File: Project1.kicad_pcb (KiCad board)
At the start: 2 copper layers, 49 parts, among them IC1 LM324N, IC2 LM324N, IC3 LM324N, IC4 LM324N

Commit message: 0518 final edited.
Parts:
- moved R19 65.0 mm to (43.7, 59.3)
- moved R20 65.0 mm to (43.7, 61.8)
- moved R21 60.1 mm to (47.7, 41.7)
- moved R22 60.1 mm to (47.7, 44.2)
- moved R23 60.1 mm to (47.7, 46.7)
- moved R24 60.1 mm to (47.7, 49.2)
- moved C6 59.8 mm to (31.7, 54.3)
- moved C7 59.8 mm to (31.7, 56.8)
- moved C8 59.8 mm to (31.7, 59.3)
- moved R10 59.8 mm to (39.7, 59.3)
- moved R8 59.8 mm to (39.7, 54.3)
- moved R9 59.8 mm to (39.7, 56.8)
- moved C5 59.8 mm to (31.7, 51.8)
- moved C9 59.8 mm to (31.7, 61.8)
- moved R11 59.8 mm to (39.7, 61.8)
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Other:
- board outline added: 100 x 100 mm

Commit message: 0520 Edited.
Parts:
- removed BZ1: Buzzer, Buzzer_Beeper:Buzzer_12x9.5RM7.6
- removed S1, S2, S3, S4: DS01-254-L-01BE, Project1:SW_DS01-254-L-01BE
- added D1: LED, LED_THT:LED_D3.0mm, F.Cu at (51.0, 35.9)
- added D2: LED, LED_THT:LED_D3.0mm, F.Cu at (51.0, 41.3)
- added D3: LED, LED_THT:LED_D3.0mm, F.Cu at (51.0, 46.8)
- added D4: LED, LED_THT:LED_D3.0mm, F.Cu at (51.0, 52.3)
- added IC5: LM324N, Project1:LM324N, F.Cu at (62.5, 22.8)
- added IC6: LM324N, Project1:LM324N, F.Cu at (73.4, 22.8)
- added Q1: Q_NPN, Project1:TNPN_TO-92_ONS, F.Cu at (42.4, 36.0)
- added Q2: Q_NPN, Project1:TNPN_TO-92_ONS, F.Cu at (42.4, 41.8)
- added Q3: Q_NPN, Project1:TNPN_TO-92_ONS, F.Cu at (42.4, 47.7)
- added Q4: Q_NPN, Project1:TNPN_TO-92_ONS, F.Cu at (42.4, 53.5)
- added R0: R, Resistor_SMD:R_0603_1608Metric, F.Cu at (19.1, 44.4)
- added R25: R, Resistor_SMD:R_0603_1608Metric, F.Cu at (27.2, 46.9)
- added R26: R, Resistor_SMD:R_0603_1608Metric, F.Cu at (27.2, 49.5)
- added R27: R, Resistor_SMD:R_0603_1608Metric, F.Cu at (27.2, 52.0)
- added R28: R, Resistor_SMD:R_0603_1608Metric, F.Cu at (27.2, 54.5)
- added R29: R, Resistor_SMD:R_0603_1608Metric, F.Cu at (27.2, 57.0)
- added R30: R, Resistor_SMD:R_0603_1608Metric, F.Cu at (27.2, 59.5)
- added R31: R, Resistor_SMD:R_0603_1608Metric, F.Cu at (27.2, 62.0)
- added R32: R, Resistor_SMD:R_0603_1608Metric, F.Cu at (31.2, 34.4)
- added R33: R, Resistor_SMD:R_0603_1608Metric, F.Cu at (31.2, 36.9)
- added R34: R, Resistor_SMD:R_0603_1608Metric, F.Cu at (31.2, 39.4)
- added R35: R, Resistor_SMD:R_0603_1608Metric, F.Cu at (31.2, 41.9)
- added R36: R, Resistor_SMD:R_0603_1608Metric, F.Cu at (31.2, 44.4)
- added R37: R, Resistor_SMD:R_0603_1608Metric, F.Cu at (31.2, 46.9)
- added R38: R, Resistor_SMD:R_0603_1608Metric, F.Cu at (31.2, 49.5)
- added R39: R, Resistor_SMD:R_0603_1608Metric, F.Cu at (31.2, 52.0)
- added R40: R, Resistor_SMD:R_0603_1608Metric, F.Cu at (31.2, 54.5)
- added R41: R, Resistor_SMD:R_0603_1608Metric, F.Cu at (31.2, 57.0)
- added R42: R, Resistor_SMD:R_0603_1608Metric, F.Cu at (31.2, 59.5)
- added R43: R, Resistor_SMD:R_0603_1608Metric, F.Cu at (31.2, 62.0)
- added R44: R, Resistor_SMD:R_0603_1608Metric, F.Cu at (35.2, 34.4)
- added R45: R, Resistor_SMD:R_0603_1608Metric, F.Cu at (35.2, 36.9)
- added R46: R, Resistor_SMD:R_0603_1608Metric, F.Cu at (35.2, 39.4)
- added R47: R, Resistor_SMD:R_0603_1608Metric, F.Cu at (35.2, 41.9)
- added R48: R, Resistor_SMD:R_0603_1608Metric, F.Cu at (35.2, 44.4)
- added R49: R, Resistor_SMD:R_0603_1608Metric, F.Cu at (35.2, 46.9)
- added R50: R, Resistor_SMD:R_0603_1608Metric, F.Cu at (35.2, 49.5)
- added R51: R, Resistor_SMD:R_0603_1608Metric, F.Cu at (35.2, 52.0)
- added R52: R, Resistor_SMD:R_0603_1608Metric, F.Cu at (35.2, 54.5)
- added R53: R, Resistor_SMD:R_0603_1608Metric, F.Cu at (35.2, 57.0)
- added R54: R, Resistor_SMD:R_0603_1608Metric, F.Cu at (35.2, 59.5)
- added R55: R, Resistor_SMD:R_0603_1608Metric, F.Cu at (35.2, 62.0)
- added R56: R, Resistor_SMD:R_0603_1608Metric, F.Cu at (39.2, 34.4)
- added R57: R, Resistor_SMD:R_0603_1608Metric, F.Cu at (39.2, 36.9)
- added R58: R, Resistor_SMD:R_0603_1608Metric, F.Cu at (39.2, 39.4)
- added R59: R, Resistor_SMD:R_0603_1608Metric, F.Cu at (39.2, 41.9)
- added R60: R, Resistor_SMD:R_0603_1608Metric, F.Cu at (39.2, 44.4)
- added R61: R, Resistor_SMD:R_0603_1608Metric, F.Cu at (39.2, 46.9)
- added R62: R, Resistor_SMD:R_0603_1608Metric, F.Cu at (39.2, 49.5)
- added R63: R, Resistor_SMD:R_0603_1608Metric, F.Cu at (39.2, 52.0)
- moved R20 32.0 mm to (27.2, 34.4)
- moved R10 25.9 mm to (23.1, 39.4)
- moved R8 25.9 mm to (23.1, 34.4)
- moved R9 25.9 mm to (23.1, 36.9)
- moved R11 25.9 mm to (23.1, 41.9)
- moved C11 25.6 mm to (15.1, 59.5)
- moved C10 25.6 mm to (15.1, 57.0)
- moved C12 25.6 mm to (15.1, 62.0)
- moved R3 23.0 mm to (19.1, 52.0)
- moved R4 23.0 mm to (19.1, 54.5)
- moved R6 23.0 mm to (19.1, 59.5)
- moved R7 23.0 mm to (19.1, 62.0)
- moved R5 23.0 mm to (19.1, 57.0)
- moved C15 22.2 mm to (19.1, 39.4)
- moved C13 22.2 mm to (19.1, 34.4)
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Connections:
- C1 pad 1: Net-(IC1-INPUT_2+) -> Net-(C1-Pad1)
- C1 pad 2: Net-(C1-Pad2) -> Net-(IC1-INPUT_3+)
- C10 pad 2: Net-(IC3-INPUT_1-) -> Net-(IC4-INPUT_2-)
- C11 pad 2: Net-(IC3-INPUT_4+) -> Net-(IC4-INPUT_4-)
- C12 pad 2: Net-(IC3-INPUT_3-) -> Net-(IC4-INPUT_3+)
- C13 pad 1: Net-(IC4-INPUT_2+) -> Net-(IC6-INPUT_2-)
- C14 pad 2: Net-(IC4-INPUT_1-) -> Net-(IC6-INPUT_2-)
- C15 pad 2: Net-(IC4-INPUT_4+) -> Net-(IC6-INPUT_4-)
- C16 pad 2: Net-(IC4-INPUT_3-) -> Net-(IC6-INPUT_3+)
- C2 pad 1: Net-(C1-Pad2) -> Net-(C1-Pad1)
- C2 pad 2: Net-(IC1-INPUT_1-) -> Net-(IC1-INPUT_4-)
- C3 pad 2: Net-(IC1-INPUT_4+) -> Net-(IC1-INPUT_2-)
- C4 pad 1: Net-(C3-Pad1) -> Net-(IC1-OUTPUT_2)
- C4 pad 2: Net-(IC1-INPUT_3-) -> Net-(C3-Pad1)
- C5 pad 1: Net-(IC2-INPUT_2+) -> Net-(IC3-INPUT_2-)
- C6 pad 2: Net-(IC2-INPUT_1-) -> Net-(IC3-INPUT_2-)
- C7 pad 2: Net-(IC2-INPUT_4+) -> Net-(IC3-INPUT_4-)
- C8 pad 2: Net-(IC2-INPUT_3-) -> Net-(IC3-INPUT_3+)
- C9 pad 1: Net-(IC3-INPUT_2+) -> Net-(IC4-OUTPUT_2)
- IC1 pad 1: Net-(IC1-INPUT_2+) -> Net-(IC1-INPUT_1-)
- IC1 pad 10: GND -> Net-(IC1-INPUT_3+)
- IC1 pad 11: GND -> -12V
- IC1 pad 12: Net-(IC1-INPUT_4+) -> GND
- IC1 pad 13: Net-(BZ1-+) -> Net-(IC1-INPUT_4-)
- IC1 pad 14: Net-(BZ1-+) -> Net-(IC1-INPUT_3+)
- IC1 pad 3: GND -> Net-(IC1-INPUT_1+)
- IC1 pad 4: +15V -> +12V
- IC1 pad 5: Net-(IC1-INPUT_2+) -> GND
- IC1 pad 7: Net-(IC1-INPUT_2-) -> Net-(IC1-OUTPUT_2)
- IC1 pad 8: Net-(IC1-INPUT_4+) -> Net-(IC1-INPUT_3-)
- IC2 pad 1: Net-(IC2-INPUT_2+) -> Net-(IC2-INPUT_1-)
- IC2 pad 10: GND -> Net-(IC2-INPUT_3+)
- IC2 pad 11: GND -> -12V
- IC2 pad 12: Net-(IC2-INPUT_4+) -> GND
- IC2 pad 13: Net-(BZ1-+) -> Net-(IC2-INPUT_4-)
- IC2 pad 14: Net-(BZ1-+) -> Net-(D1-A)
- IC2 pad 3: GND -> Net-(IC2-INPUT_1+)
- IC2 pad 4: +15V -> +12V
- IC2 pad 5: Net-(IC2-INPUT_2+) -> GND
- IC2 pad 7: Net-(IC2-INPUT_2-) -> Net-(D2-A)
- IC2 pad 8: Net-(IC2-INPUT_4+) -> Net-(IC2-INPUT_3-)
- IC3 pad 1: Net-(IC3-INPUT_2+) -> Net-(IC3-INPUT_1-)
- IC3 pad 10: GND -> Net-(IC3-INPUT_3+)
- IC3 pad 11: GND -> -12V
- IC3 pad 12: Net-(IC3-INPUT_4+) -> GND
- IC3 pad 13: Net-(BZ1-+) -> Net-(IC3-INPUT_4-)
- IC3 pad 14: Net-(BZ1-+) -> Net-(IC3-INPUT_3+)
- IC3 pad 3: GND -> Net-(IC3-INPUT_1+)
- IC3 pad 4: +15V -> +12V
- IC3 pad 5: Net-(IC3-INPUT_2+) -> GND
- IC3 pad 8: Net-(IC3-INPUT_4+) -> Net-(IC3-INPUT_3-)
- IC4 pad 1: Net-(IC4-INPUT_2+) -> Net-(IC4-INPUT_1-)
- IC4 pad 10: GND -> Net-(IC4-INPUT_3+)
- IC4 pad 11: GND -> -12V
- IC4 pad 12: Net-(IC4-INPUT_4+) -> GND
- IC4 pad 13: Net-(BZ1-+) -> Net-(IC4-INPUT_4-)
- IC4 pad 14: Net-(BZ1-+) -> Net-(IC4-INPUT_3+)
- IC4 pad 3: GND -> Net-(IC4-INPUT_1+)
- IC4 pad 4: +15V -> +12V
- IC4 pad 5: Net-(IC4-INPUT_2+) -> GND
- IC4 pad 7: Net-(IC4-INPUT_2-) -> Net-(IC4-OUTPUT_2)
- IC4 pad 8: Net-(IC4-INPUT_4+) -> Net-(IC4-INPUT_3-)
- R1 pad 1: Net-(R1-Pad1) -> Net-(IC1-INPUT_1-)
- R1 pad 2: Net-(C1-Pad2) -> Net-(R1-Pad2)
- R10 pad 1: Net-(IC2-INPUT_2-) -> Net-(R10-Pad1)
- R10 pad 2: Net-(C7-Pad1) -> Net-(IC1-OUTPUT_2)
- R11 pad 1: Net-(C7-Pad1) -> Net-(IC2-INPUT_1+)
- R12 pad 1: Net-(IC2-INPUT_4+) -> Net-(IC2-INPUT_1+)
- R12 pad 2: Net-(IC2-INPUT_3-) -> +12V
- R13 pad 1: Net-(R13-Pad1) -> Net-(IC2-INPUT_4-)
- R13 pad 2: Net-(C10-Pad1) -> Net-(IC2-INPUT_1-)
- R14 pad 1: Net-(C10-Pad1) -> Net-(IC2-INPUT_4-)
- R14 pad 2: GND -> -12V
- R15 pad 1: Net-(IC3-INPUT_2+) -> Net-(IC2-INPUT_4-)
- R15 pad 2: Net-(IC3-INPUT_1-) -> Net-(D1-A)
- R16 pad 1: Net-(IC3-INPUT_2-) -> Net-(R16-Pad1)
- R16 pad 2: Net-(C11-Pad1) -> Net-(IC3-INPUT_2-)
- R17 pad 1: Net-(C11-Pad1) -> Net-(IC3-INPUT_2-)
- R17 pad 2: GND -> Net-(R16-Pad1)
- R18 pad 1: Net-(IC3-INPUT_4+) -> Net-(R0-Pad1)
- R18 pad 2: Net-(IC3-INPUT_3-) -> Net-(IC3-INPUT_1+)
- R19 pad 1: Net-(R19-Pad1) -> Net-(IC2-INPUT_3+)
- R19 pad 2: Net-(C13-Pad2) -> +12V
- R2 pad 1: Net-(C1-Pad2) -> Net-(R1-Pad2)
- R2 pad 2: GND -> Net-(C1-Pad1)
- R20 pad 1: Net-(C13-Pad2) -> Net-(IC2-INPUT_3+)
- R21 pad 1: Net-(IC4-INPUT_2+) -> Net-(IC3-INPUT_1-)
- R21 pad 2: Net-(IC4-INPUT_1-) -> Net-(R21-Pad2)
- R22 pad 1: Net-(IC4-INPUT_2-) -> Net-(C5-Pad2)
- R22 pad 2: Net-(C15-Pad1) -> GND
- R23 pad 1: Net-(C15-Pad1) -> Net-(R23-Pad1)
- R23 pad 2: GND -> Net-(IC4-OUTPUT_2)
- R24 pad 1: Net-(IC4-INPUT_4+) -> Net-(R21-Pad2)
- R24 pad 2: Net-(IC4-INPUT_3-) -> Net-(C7-Pad1)
- R3 pad 1: Net-(IC1-INPUT_2+) -> Net-(C1-Pad1)
- R3 pad 2: Net-(IC1-INPUT_1-) -> GND
- R4 pad 1: Net-(IC1-INPUT_2-) -> Net-(R4-Pad1)
- R4 pad 2: Net-(C3-Pad1) -> Net-(IC1-INPUT_3+)
- R5 pad 1: Net-(C3-Pad1) -> Net-(IC1-INPUT_4-)
- R5 pad 2: GND -> Net-(R4-Pad1)
- R6 pad 1: Net-(IC1-INPUT_4+) -> Net-(IC1-INPUT_3-)
- R6 pad 2: Net-(IC1-INPUT_3-) -> Net-(R6-Pad2)
- R7 pad 1: Net-(R7-Pad1) -> Net-(R6-Pad2)
- R7 pad 2: Net-(C5-Pad2) -> Net-(C3-Pad1)
- R8 pad 1: Net-(C5-Pad2) -> Net-(C3-Pad1)
- R9 pad 1: Net-(IC2-INPUT_2+) -> Net-(IC1-INPUT_2-)
- R9 pad 2: Net-(IC2-INPUT_1-) -> Net-(R10-Pad1)

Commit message: 0523 Edited.
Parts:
- removed R0: R, Resistor_SMD:R_0603_1608Metric
- added D5: LED, LED_THT:LED_D3.0mm, F.Cu at (34.1, 57.0)
- added D6: LED, LED_THT:LED_D3.0mm, F.Cu at (34.1, 62.4)
- added D7: LED, LED_THT:LED_D3.0mm, F.Cu at (40.0, 57.0)
- added D8: LED, LED_THT:LED_D3.0mm, F.Cu at (40.0, 62.4)
- added IC7: LM324N, Project1:LM324N, F.Cu at (83.3, 23.3)
- added MK1: Microphone, Project1:MIC_CMA-4544PF-W, F.Cu at (72.5, 39.2)
- added Q5: NPN, Project1:TO-92_FAS_NPN, F.Cu at (15.9, 63.1)
- added Q6: NPN, Project1:TO-92_FAS_NPN, F.Cu at (15.9, 69.3)
- added Q7: NPN, Project1:TO-92_FAS_NPN, F.Cu at (15.9, 75.5)
- added Q8: NPN, Project1:TO-92_FAS_NPN, F.Cu at (15.9, 81.7)
- added R64: R, Resistor_SMD:R_0201_0603Metric, F.Cu at (65.7, 38.0)
- added R65: R, Resistor_SMD:R_0201_0603Metric, F.Cu at (65.7, 39.8)
- added R66: R, Resistor_SMD:R_0201_0603Metric, F.Cu at (65.7, 41.5)
- added R67: R, Resistor_SMD:R_0201_0603Metric, F.Cu at (65.7, 43.2)
- added R68: R, Resistor_SMD:R_0201_0603Metric, F.Cu at (65.7, 45.0)
- added R69: R, Resistor_SMD:R_0201_0603Metric, F.Cu at (65.7, 46.8)
- added R70: R, Resistor_SMD:R_0201_0603Metric, F.Cu at (65.7, 48.5)
- added R71: R, Resistor_SMD:R_0201_0603Metric, F.Cu at (65.7, 50.2)
- added R72: R, Resistor_SMD:R_0201_0603Metric, F.Cu at (65.7, 52.0)
- added RV1: R_Potentiometer_Trim, Project1:TRIM_TC33X-2-101E, F.Cu at (24.3, 36.2)
- added RV10: R_Potentiometer_Trim, Project1:TRIM_TC33X-2-101E, F.Cu at (37.6, 41.4)
- added RV11: R_Potentiometer_Trim, Project1:TRIM_TC33X-2-101E, F.Cu at (37.6, 46.5)
- added RV12: R_Potentiometer_Trim, Project1:TRIM_TC33X-2-101E, F.Cu at (37.6, 51.6)
- added RV13: R_Potentiometer_Trim, Project1:TRIM_TC33X-2-101E, F.Cu at (44.3, 36.2)
- added RV14: R_Potentiometer_Trim, Project1:TRIM_TC33X-2-101E, F.Cu at (44.3, 41.4)
- added RV15: R_Potentiometer_Trim, Project1:TRIM_TC33X-2-101E, F.Cu at (44.3, 46.5)
- added RV16: R_Potentiometer_Trim, Project1:TRIM_TC33X-2-101E, F.Cu at (44.3, 51.6)
- added RV2: R_Potentiometer_Trim, Project1:TRIM_TC33X-2-101E, F.Cu at (24.3, 41.4)
- added RV3: R_Potentiometer_Trim, Project1:TRIM_TC33X-2-101E, F.Cu at (24.3, 46.5)
- added RV4: R_Potentiometer_Trim, Project1:TRIM_TC33X-2-101E, F.Cu at (24.3, 51.6)
- added RV5: R_Potentiometer_Trim, Project1:TRIM_TC33X-2-101E, F.Cu at (31.0, 36.2)
- added RV6: R_Potentiometer_Trim, Project1:TRIM_TC33X-2-101E, F.Cu at (31.0, 41.4)
- added RV7: R_Potentiometer_Trim, Project1:TRIM_TC33X-2-101E, F.Cu at (31.0, 46.5)
- added RV8: R_Potentiometer_Trim, Project1:TRIM_TC33X-2-101E, F.Cu at (31.0, 51.6)
- added RV9: R_Potentiometer_Trim, Project1:TRIM_TC33X-2-101E, F.Cu at (37.6, 36.2)
- C1, C10, C11, C12, C13, C14, C15, C16, C2, C3, C4, C5, C6, C7, C8, C9: footprint Capacitor_SMD:C_0603_1608Metric -> Capacitor_SMD:C_0201_0603Metric
- Q1, Q2, Q3, Q4: value Q_NPN -> NPN; footprint Project1:TNPN_TO-92_ONS -> Project1:TO-92_FAS_NPN
- R1, R10, R11, R12, R13, R14, R15, R16, R17, R18, R19, R2, R20, R21, R22, R23, R24, R25, R26, R27, R28, R29, R3, R30, R31, R32, R33, R34, R35, R36, R37, R38, R39, R4, R40, R41, R42, R43, R44, R45, R46, R47, R48, R49, R5, R50, R51, R52, R53, R54, R55, R56, R57, R58, R59, R6, R60, R61, R62, R63, R7, R8, R9: footprint Resistor_SMD:R_0603_1608Metric -> Resistor_SMD:R_0201_0603Metric
- moved C12 45.2 mm to (51.0, 34.5)
- moved R7 43.9 mm to (53.4, 34.5)
- moved R19 41.6 mm to (55.9, 36.2)
- moved R18 41.2 mm to (55.9, 34.5)
- moved R31 39.3 mm to (58.3, 38.0)
- moved R30 38.9 mm to (58.3, 36.2)
- moved R29 38.4 mm to (58.3, 34.5)
- moved R43 37.0 mm to (60.8, 39.8)
- moved R42 36.6 mm to (60.8, 38.0)
- moved R41 36.1 mm to (60.8, 36.2)
- moved R40 35.7 mm to (60.8, 34.5)
- moved D1 35.6 mm to (22.3, 57.0)
- moved D2 35.6 mm to (22.3, 62.4)
- moved R55 34.7 mm to (63.2, 41.5)
- moved R54 34.3 mm to (63.2, 39.8)
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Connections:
- C1 pad 2: Net-(IC1-INPUT_3+) -> Net-(IC1-INPUT_1-)
- C10 pad 2: Net-(IC4-INPUT_2-) -> Net-(IC5-INPUT_1-)
- C11 pad 2: Net-(IC4-INPUT_4-) -> Net-(IC5-INPUT_2-)
- C12 pad 2: Net-(IC4-INPUT_3+) -> Net-(IC5-OUTPUT_2)
- C13 pad 1: Net-(IC6-INPUT_2-) -> Net-(C13-Pad1)
- C13 pad 2: Net-(C13-Pad2) -> Net-(IC5-OUTPUT_4)
- C14 pad 1: Net-(C13-Pad2) -> Net-(C13-Pad1)
- C14 pad 2: Net-(IC6-INPUT_2-) -> Net-(IC5-INPUT_4-)
- C15 pad 2: Net-(IC6-INPUT_4-) -> Net-(IC5-INPUT_3-)
- C16 pad 2: Net-(IC6-INPUT_3+) -> Net-(IC5-OUTPUT_3)
- C2 pad 2: Net-(IC1-INPUT_4-) -> Net-(IC1-OUTPUT_1)
- C3 pad 2: Net-(IC1-INPUT_2-) -> Net-(IC1-OUTPUT_2)
- C4 pad 1: Net-(IC1-OUTPUT_2) -> Net-(C3-Pad1)
- C4 pad 2: Net-(C3-Pad1) -> Net-(IC1-INPUT_2-)
- C5 pad 1: Net-(IC3-INPUT_2-) -> Net-(C5-Pad1)
- C5 pad 2: Net-(C5-Pad2) -> Net-(IC1-OUTPUT_4)
- C6 pad 1: Net-(C5-Pad2) -> Net-(C5-Pad1)
- C6 pad 2: Net-(IC3-INPUT_2-) -> Net-(IC1-INPUT_4-)
- C7 pad 2: Net-(IC3-INPUT_4-) -> Net-(IC1-OUTPUT_3)
- C8 pad 2: Net-(IC3-INPUT_3+) -> Net-(IC1-INPUT_3-)
- C9 pad 1: Net-(IC4-OUTPUT_2) -> Net-(C10-Pad1)
- C9 pad 2: Net-(C10-Pad1) -> Net-(IC5-OUTPUT_1)
- IC1 pad 1: Net-(IC1-INPUT_1-) -> Net-(IC1-OUTPUT_1)
- IC1 pad 10: Net-(IC1-INPUT_3+) -> GND
- IC1 pad 14: Net-(IC1-INPUT_3+) -> Net-(IC1-OUTPUT_4)
- IC1 pad 3: Net-(IC1-INPUT_1+) -> GND
- IC1 pad 8: Net-(IC1-INPUT_3-) -> Net-(IC1-OUTPUT_3)
- IC2 pad 1: Net-(IC2-INPUT_1-) -> Net-(D1-A)
- IC2 pad 14: Net-(D1-A) -> Net-(D4-A)
- IC2 pad 3: Net-(IC2-INPUT_1+) -> GND
- IC2 pad 5: GND -> Net-(IC2-INPUT_2+)
- IC2 pad 7: Net-(D2-A) -> Net-(IC2-INPUT_2-)
- IC3 pad 1: Net-(IC3-INPUT_1-) -> Net-(D2-A)
- IC3 pad 14: Net-(IC3-INPUT_3+) -> Net-(D3-A)
- IC3 pad 3: Net-(IC3-INPUT_1+) -> GND
- IC3 pad 5: GND -> Net-(IC3-INPUT_2+)
- IC4 pad 1: Net-(IC4-INPUT_1-) -> Net-(D5-A)
- IC4 pad 14: Net-(IC4-INPUT_3+) -> Net-(D8-A)
- IC4 pad 3: Net-(IC4-INPUT_1+) -> GND
- IC4 pad 5: GND -> Net-(IC4-INPUT_2+)
- IC4 pad 7: Net-(IC4-OUTPUT_2) -> Net-(IC4-INPUT_2-)
- IC5 pad 1: Net-(IC5-INPUT_1-) -> Net-(IC5-OUTPUT_1)
- IC5 pad 10: Net-(IC5-INPUT_3+) -> GND
- IC5 pad 14: Net-(D3-A) -> Net-(IC5-OUTPUT_4)
- IC5 pad 3: Net-(IC5-INPUT_1+) -> GND
- IC5 pad 7: Net-(D4-A) -> Net-(IC5-OUTPUT_2)
- IC5 pad 8: Net-(IC5-INPUT_3-) -> Net-(IC5-OUTPUT_3)
- IC6 pad 1: Net-(IC6-INPUT_1-) -> Net-(D6-A)
- IC6 pad 14: Net-(IC6-INPUT_3+) -> Net-(D7-A)
- IC6 pad 3: Net-(IC6-INPUT_1+) -> GND
- IC6 pad 5: GND -> Net-(IC6-INPUT_2+)
- Q1 pad 1: (no net) -> Net-(IC2-INPUT_2+)
- Q1 pad 2: (no net) -> Net-(Q1-B)
- Q1 pad 3: (no net) -> GND
- Q2 pad 1: (no net) -> Net-(IC2-INPUT_3+)
- Q2 pad 2: (no net) -> Net-(Q2-B)
- Q2 pad 3: (no net) -> GND
- Q3 pad 1: (no net) -> Net-(IC3-INPUT_3+)
- Q3 pad 2: (no net) -> Net-(Q3-B)
- Q3 pad 3: (no net) -> GND
- Q4 pad 1: (no net) -> Net-(IC3-INPUT_2+)
- Q4 pad 2: (no net) -> Net-(Q4-B)
- Q4 pad 3: (no net) -> GND
- R1 pad 1: Net-(IC1-INPUT_1-) -> Net-(IC7-INPUT_4-)
- R1 pad 2: Net-(R1-Pad2) -> Net-(C1-Pad1)
- R10 pad 1: Net-(R10-Pad1) -> Net-(IC2-INPUT_2+)
- R10 pad 2: Net-(IC1-OUTPUT_2) -> GND
- R11 pad 1: Net-(IC2-INPUT_1+) -> +12V
- R11 pad 2: GND -> Net-(IC2-INPUT_2+)
- R12 pad 1: Net-(IC2-INPUT_1+) -> Net-(IC2-INPUT_1-)
- R12 pad 2: +12V -> Net-(IC2-INPUT_2-)
- R13 pad 1: Net-(IC2-INPUT_4-) -> -12V
- R14 pad 1: Net-(IC2-INPUT_4-) -> Net-(IC2-INPUT_1-)
- R14 pad 2: -12V -> Net-(D1-A)
- R15 pad 1: Net-(IC2-INPUT_4-) -> -12V
- R15 pad 2: Net-(D1-A) -> Net-(IC2-INPUT_4-)
- R16 pad 1: Net-(R16-Pad1) -> +12V
- R16 pad 2: Net-(IC3-INPUT_2-) -> Net-(IC2-INPUT_3+)
- R17 pad 1: Net-(IC3-INPUT_2-) -> Net-(IC2-INPUT_4-)
- R17 pad 2: Net-(R16-Pad1) -> Net-(D4-A)
- R18 pad 1: Net-(R0-Pad1) -> Net-(IC2-INPUT_3+)
- R18 pad 2: Net-(IC3-INPUT_1+) -> GND
- R19 pad 1: Net-(IC2-INPUT_3+) -> Net-(IC2-INPUT_4-)
- R19 pad 2: +12V -> Net-(IC2-INPUT_3-)
- R2 pad 1: Net-(R1-Pad2) -> Net-(IC1-OUTPUT_1)
- R2 pad 2: Net-(C1-Pad1) -> Net-(IC1-INPUT_1-)
- R20 pad 1: Net-(IC2-INPUT_3+) -> Net-(Q2-B)
- R20 pad 2: GND -> Net-(R20-Pad2)
- R21 pad 1: Net-(IC3-INPUT_1-) -> -12V
- R21 pad 2: Net-(R21-Pad2) -> Net-(IC4-INPUT_1-)
- R22 pad 1: Net-(C5-Pad2) -> +12V
- R22 pad 2: GND -> Net-(IC3-INPUT_3+)
- R23 pad 1: Net-(R23-Pad1) -> Net-(IC4-INPUT_1-)
- R23 pad 2: Net-(IC4-OUTPUT_2) -> Net-(D5-A)
- R24 pad 1: Net-(R21-Pad2) -> Net-(IC3-INPUT_3+)
- R24 pad 2: Net-(C7-Pad1) -> GND
- R25 pad 1: Net-(R25-Pad1) -> Net-(IC4-INPUT_1-)
- R25 pad 2: Net-(C5-Pad2) -> Net-(IC4-INPUT_2-)
- R26 pad 1: Net-(C7-Pad1) -> Net-(Q3-B)
- R26 pad 2: GND -> Net-(R26-Pad2)
- R27 pad 1: Net-(IC3-INPUT_3-) -> Net-(Q4-B)
- R27 pad 2: Net-(R25-Pad1) -> Net-(R27-Pad2)
- R28 pad 1: Net-(IC4-INPUT_2-) -> -12V
- R28 pad 2: Net-(R23-Pad1) -> Net-(IC4-INPUT_4-)
- R29 pad 1: Net-(IC3-INPUT_4-) -> Net-(IC4-INPUT_4-)
- R29 pad 2: Net-(R29-Pad2) -> Net-(D8-A)
- R3 pad 1: Net-(C1-Pad1) -> Net-(IC7-INPUT_4-)
- R3 pad 2: GND -> Net-(C3-Pad1)
- R30 pad 1: Net-(R29-Pad2) -> Net-(IC3-INPUT_2+)
- R30 pad 2: Net-(IC3-INPUT_3+) -> GND
- R31 pad 1: Net-(R0-Pad1) -> +12V
- R31 pad 2: Net-(IC4-INPUT_1+) -> Net-(IC3-INPUT_2+)
- R32 pad 1: Net-(IC2-INPUT_2-) -> Net-(IC4-INPUT_4-)
- R32 pad 2: Net-(IC2-INPUT_3-) -> Net-(IC4-INPUT_3-)
- R33 pad 1: Net-(IC2-INPUT_2-) -> Net-(IC7-INPUT_4-)
- R33 pad 2: -12V -> Net-(C10-Pad1)
- R34 pad 1: Net-(IC2-INPUT_2-) -> Net-(IC7-INPUT_4-)
- R34 pad 2: Net-(D2-A) -> Net-(C11-Pad1)
- R35 pad 1: Net-(IC5-INPUT_1+) -> -12V
- R35 pad 2: +12V -> Net-(IC3-INPUT_1-)
- R36 pad 1: Net-(IC5-INPUT_1+) -> Net-(IC3-INPUT_1-)
- R36 pad 2: GND -> Net-(D2-A)
- R37 pad 1: Net-(IC4-INPUT_1-) -> +12V
- R37 pad 2: Net-(R37-Pad2) -> Net-(IC4-INPUT_2+)
- R38 pad 1: Net-(C10-Pad1) -> +12V
- R38 pad 2: GND -> Net-(IC6-INPUT_2+)
- R39 pad 1: Net-(IC5-INPUT_4-) -> Net-(IC5-OUTPUT_1)
- R4 pad 1: Net-(R4-Pad1) -> Net-(IC1-OUTPUT_2)
- R4 pad 2: Net-(IC1-INPUT_3+) -> Net-(IC1-INPUT_2-)
- R40 pad 1: Net-(IC5-INPUT_2-) -> Net-(IC5-OUTPUT_2)
- R40 pad 2: Net-(D4-A) -> Net-(IC5-INPUT_2-)
- R41 pad 1: Net-(R37-Pad2) -> Net-(IC3-INPUT_1-)
- R41 pad 2: Net-(C11-Pad1) -> Net-(IC3-INPUT_2-)
- R42 pad 1: Net-(R42-Pad1) -> Net-(IC4-INPUT_2+)
- R42 pad 2: Net-(C10-Pad1) -> GND
- R43 pad 1: Net-(C11-Pad1) -> Net-(IC6-INPUT_2+)
- R44 pad 1: Net-(IC4-INPUT_3-) -> -12V
- R44 pad 2: Net-(R42-Pad1) -> Net-(IC3-INPUT_4-)
- R45 pad 1: Net-(IC5-INPUT_4-) -> Net-(IC3-INPUT_4-)
- R45 pad 2: -12V -> Net-(D3-A)
- R46 pad 1: Net-(IC5-INPUT_2-) -> Net-(IC3-INPUT_4-)
- R46 pad 2: -12V -> Net-(IC3-INPUT_3-)
- R47 pad 1: Net-(IC4-INPUT_4-) -> Net-(Q5-B)
- R48 pad 1: Net-(R47-Pad2) -> Net-(Q6-B)
- R48 pad 2: Net-(IC4-INPUT_3+) -> Net-(R48-Pad2)
- R49 pad 1: Net-(IC5-INPUT_4-) -> Net-(Q7-B)
- R49 pad 2: Net-(D3-A) -> Net-(R49-Pad2)
- R5 pad 1: Net-(IC1-INPUT_4-) -> Net-(IC7-INPUT_4-)
- R5 pad 2: Net-(R4-Pad1) -> Net-(C5-Pad1)
- R50 pad 1: Net-(IC5-INPUT_2-) -> Net-(Q8-B)
- R50 pad 2: Net-(IC5-INPUT_3-) -> Net-(R50-Pad2)
- R51 pad 1: Net-(IC5-INPUT_3+) -> -12V
- R51 pad 2: GND -> Net-(IC6-INPUT_4-)
- R52 pad 1: Net-(IC5-INPUT_3+) -> Net-(IC6-INPUT_4-)
- R52 pad 2: +12V -> Net-(D7-A)
- R53 pad 1: Net-(R53-Pad1) -> Net-(IC6-INPUT_4-)
- R53 pad 2: Net-(IC6-INPUT_2-) -> Net-(IC6-INPUT_3-)
- R54 pad 1: Net-(IC6-INPUT_2-) -> Net-(IC4-INPUT_3+)
- R54 pad 2: Net-(R53-Pad1) -> GND
- R55 pad 1: Net-(R0-Pad1) -> Net-(IC6-INPUT_3+)
- R55 pad 2: Net-(IC6-INPUT_1+) -> GND
- R56 pad 1: Net-(IC6-INPUT_1-) -> -12V
- R56 pad 2: Net-(R56-Pad2) -> Net-(IC6-INPUT_1-)
- R57 pad 1: Net-(C13-Pad2) -> Net-(IC5-OUTPUT_4)
- R57 pad 2: GND -> Net-(IC5-INPUT_4-)
- R58 pad 1: Net-(R56-Pad2) -> Net-(IC5-OUTPUT_3)
- R58 pad 2: Net-(C15-Pad1) -> Net-(IC5-INPUT_3-)
- R59 pad 1: Net-(R59-Pad1) -> +12V
- R59 pad 2: Net-(C13-Pad2) -> Net-(IC4-INPUT_3+)
- R6 pad 1: Net-(IC1-INPUT_3-) -> Net-(IC1-OUTPUT_4)
- R6 pad 2: Net-(R6-Pad2) -> Net-(IC1-INPUT_4-)
- R60 pad 1: Net-(C15-Pad1) -> +12V
- R60 pad 2: GND -> Net-(IC6-INPUT_3+)
- R61 pad 1: Net-(IC6-INPUT_3-) -> Net-(IC6-INPUT_1-)
- R61 pad 2: Net-(R59-Pad1) -> Net-(D6-A)
- R62 pad 1: Net-(IC6-INPUT_4-) -> Net-(IC6-INPUT_1-)
- R62 pad 2: Net-(R62-Pad2) -> Net-(IC6-INPUT_2-)
- R63 pad 1: Net-(R62-Pad2) -> Net-(IC7-INPUT_4-)
- R63 pad 2: Net-(IC6-INPUT_3+) -> Net-(C13-Pad1)
- R7 pad 1: Net-(R6-Pad2) -> Net-(IC7-INPUT_4-)
- R7 pad 2: Net-(C3-Pad1) -> Net-(C7-Pad1)
- R8 pad 1: Net-(C3-Pad1) -> Net-(IC1-OUTPUT_3)
- R8 pad 2: GND -> Net-(IC1-INPUT_3-)
- R9 pad 1: Net-(IC1-INPUT_2-) -> Net-(Q1-B)
- R9 pad 2: Net-(R10-Pad1) -> Net-(R9-Pad2)

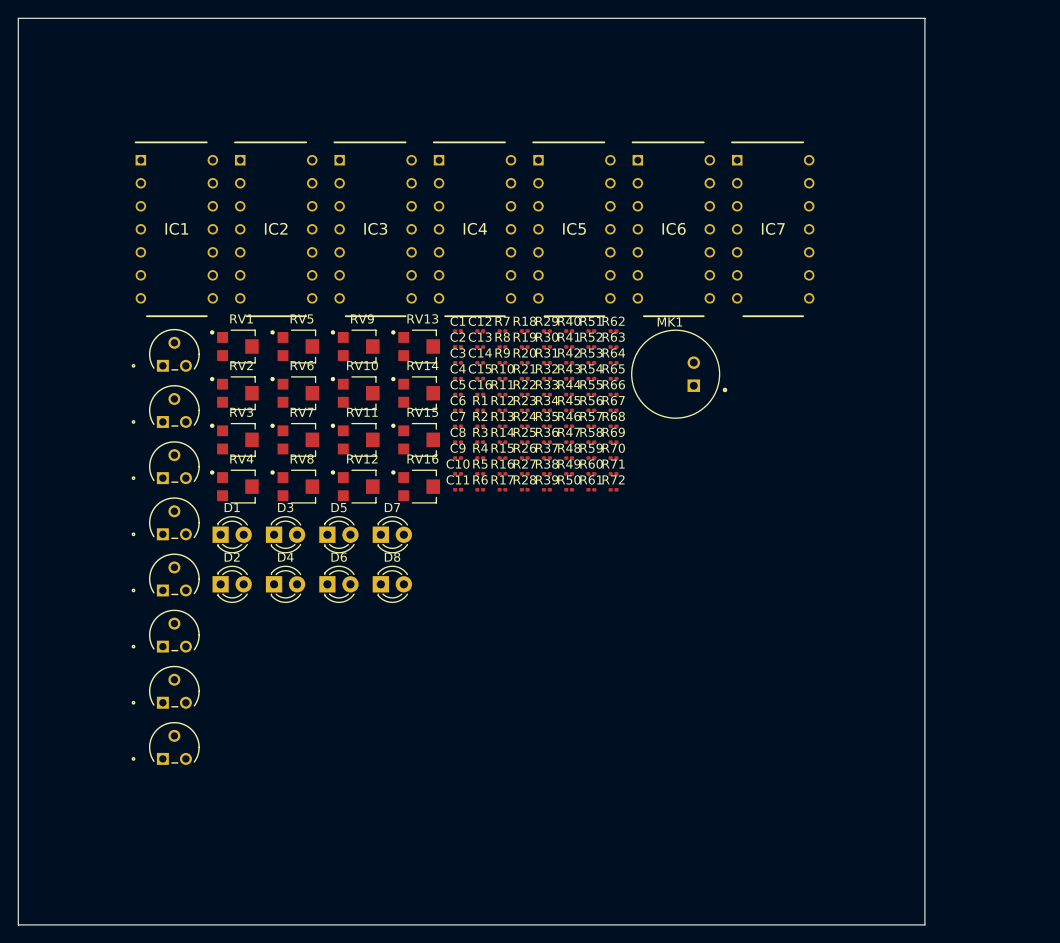
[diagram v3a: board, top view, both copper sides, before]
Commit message: add some smd resistors
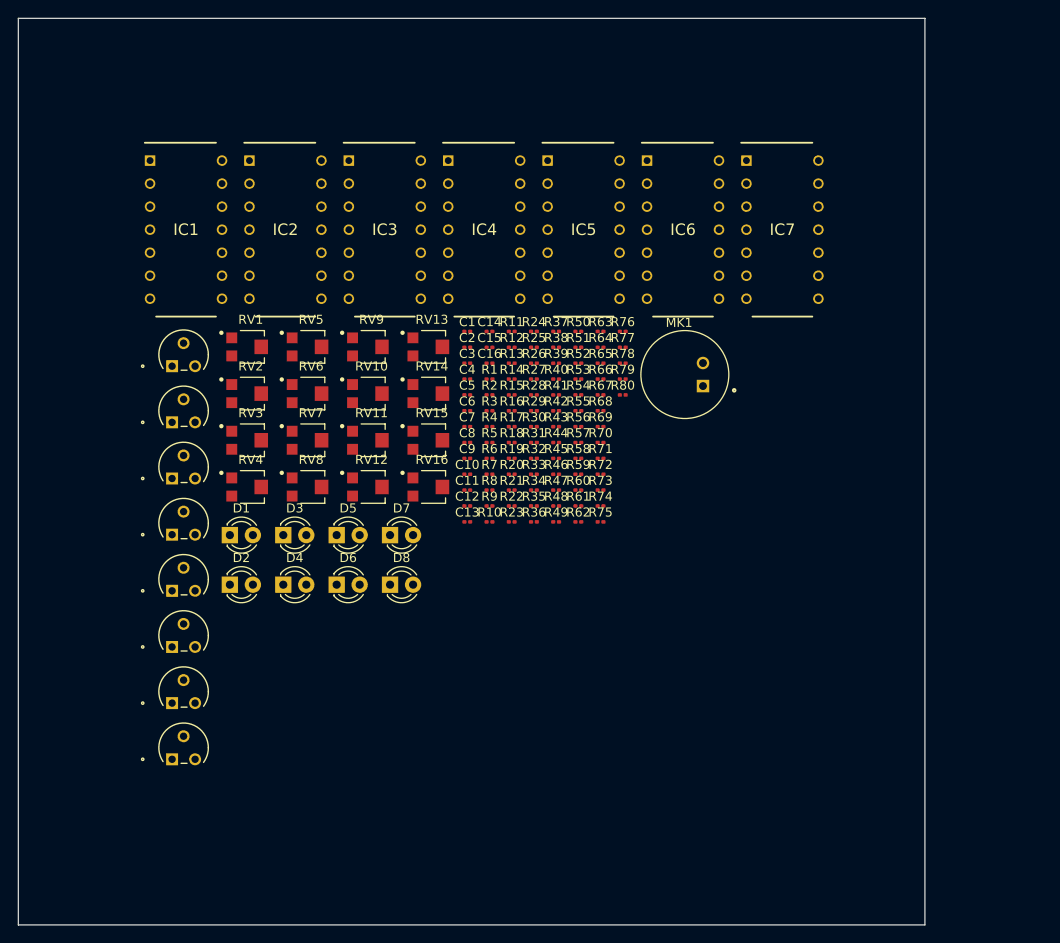
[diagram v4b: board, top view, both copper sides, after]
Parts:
- added R73: R, Resistor_SMD:R_0201_0603Metric, F.Cu at (64.2, 52.0)
- added R74: R, Resistor_SMD:R_0201_0603Metric, F.Cu at (64.2, 53.8)
- added R75: R, Resistor_SMD:R_0201_0603Metric, F.Cu at (64.2, 55.5)
- added R76: R, Resistor_SMD:R_0201_0603Metric, F.Cu at (66.7, 34.5)
- added R77: R, Resistor_SMD:R_0201_0603Metric, F.Cu at (66.7, 36.3)
- added R78: R, Resistor_SMD:R_0201_0603Metric, F.Cu at (66.7, 38.0)
- added R79: R, Resistor_SMD:R_0201_0603Metric, F.Cu at (66.7, 39.8)
- added R80: R, Resistor_SMD:R_0201_0603Metric, F.Cu at (66.7, 41.5)
- moved R62 21.4 mm to (61.8, 55.5)
- moved C12 19.3 mm to (49.5, 53.8)
- moved C13 19.3 mm to (49.5, 55.5)
- moved R50 17.5 mm to (61.8, 34.5)
- moved R10 15.9 mm to (52.0, 55.5)
- moved R7 15.9 mm to (52.0, 50.3)
- moved R8 15.9 mm to (52.0, 52.0)
- moved R9 15.9 mm to (52.0, 53.8)
- moved R37 14.0 mm to (59.3, 34.5)
- moved R38 14.0 mm to (59.3, 36.3)
- moved R39 14.0 mm to (59.3, 38.0)
- moved R18 12.4 mm to (54.4, 46.8)
- moved R19 12.4 mm to (54.4, 48.5)
- moved R20 12.4 mm to (54.4, 50.3)
- moved R21 12.4 mm to (54.4, 52.0)
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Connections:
- RV1 pad 2: Net-(C1-Pad1) -> Net-(R73-Pad1)
- RV2 pad 2: Net-(C3-Pad1) -> Net-(R75-Pad1)
- RV3 pad 2: Net-(C5-Pad1) -> Net-(R74-Pad1)
- RV4 pad 2: Net-(C7-Pad1) -> Net-(R76-Pad1)
- RV5 pad 2: Net-(C10-Pad1) -> Net-(R77-Pad1)
- RV6 pad 2: Net-(C11-Pad1) -> Net-(R80-Pad1)
- RV7 pad 2: Net-(C13-Pad1) -> Net-(R78-Pad1)
- RV8 pad 2: Net-(C15-Pad1) -> Net-(R79-Pad1)
